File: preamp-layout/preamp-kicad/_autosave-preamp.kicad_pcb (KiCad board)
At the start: 2 copper layers, 431 parts, among them J1 Screw_Terminal_01x03, J10 Conn_01x03_Male, J11 Conn_01x02_Male, J12 Conn_01x02_Male, J13 Conn_01x02_Male, J14 Screw_Terminal_01x03, J15 Conn_01x02_Male, J16 Conn_01x02_Male, J17 Conn_01x02_Female, J18 Conn_01x02_Female, J19 Conn_01x05_Female, J2 Conn_01x02_Female, J20 Conn_01x03_Male, J26 Conn_01x03_Female, J27 Conn_01x03_Female, J28 Conn_01x03_Female, J29 Conn_01x03_Female, J3 Conn_01x02_Female, J30 Conn_01x03_Female, J31 Conn_01x03_Male, J32 Conn_01x03_Male, J35 Conn_01x03_Male, J36 Conn_01x03_Male, J37 Conn_01x03_Male, J38 Conn_01x03_Male, J39 Conn_01x03_Male, J4 Conn_01x02_Male, J40 Conn_01x03_Male, J41 Conn_01x03_Male, J42 Conn_01x03_Female, J43 Conn_01x03_Female, J44 Conn_01x02_Female, J45 Conn_01x07_Female, J46 Conn_01x07_Female, J47 Conn_01x02_Male, J48 Conn_01x02_Male, J49 Conn_01x03_Female, J5 Screw_Terminal_01x03, J50 Conn_01x03_Male, J51 Conn_01x02_Male, J52 Conn_01x03_Female, J53 Conn_01x03_Female, J54 Conn_01x03_Male, J55 Conn_01x02_Male, J56 Conn_01x03_Male, J57 Conn_01x02_Male, J58 Conn_01x03_Male, J59 Conn_01x04_Male, J6 Screw_Terminal_01x03, J60 Conn_01x04_Female, J61 Conn_01x03_Male, J62 Conn_01x03_Male, J64 Conn_01x04_Female, J65 Conn_01x04_Male, J66 Conn_01x03_Male, J67 Conn_01x03_Male, J68 Conn_01x03_Female, J69 Conn_01x03_Male, J7 Screw_Terminal_01x03, J70 XLR3, J71 XLR3, J72 XLR3, J73 XLR3, J74 Conn_01x03_Female, J75 Conn_01x03_Female, J76 Conn_01x03_Female, J77 Conn_01x03_Female, J78 Conn_01x03_Female, J79 Conn_01x03_Female, J8 Conn_01x03_Male, J80 Conn_01x03_Female, J81 Conn_01x03_Female, J82 Conn_01x02_Male, J83 Conn_01x02_Male, J84 Conn_01x05_Female, J9 Conn_01x03_Male, K2 G6JU, K3 G6JU, K4 G6JU, K5 G6JU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

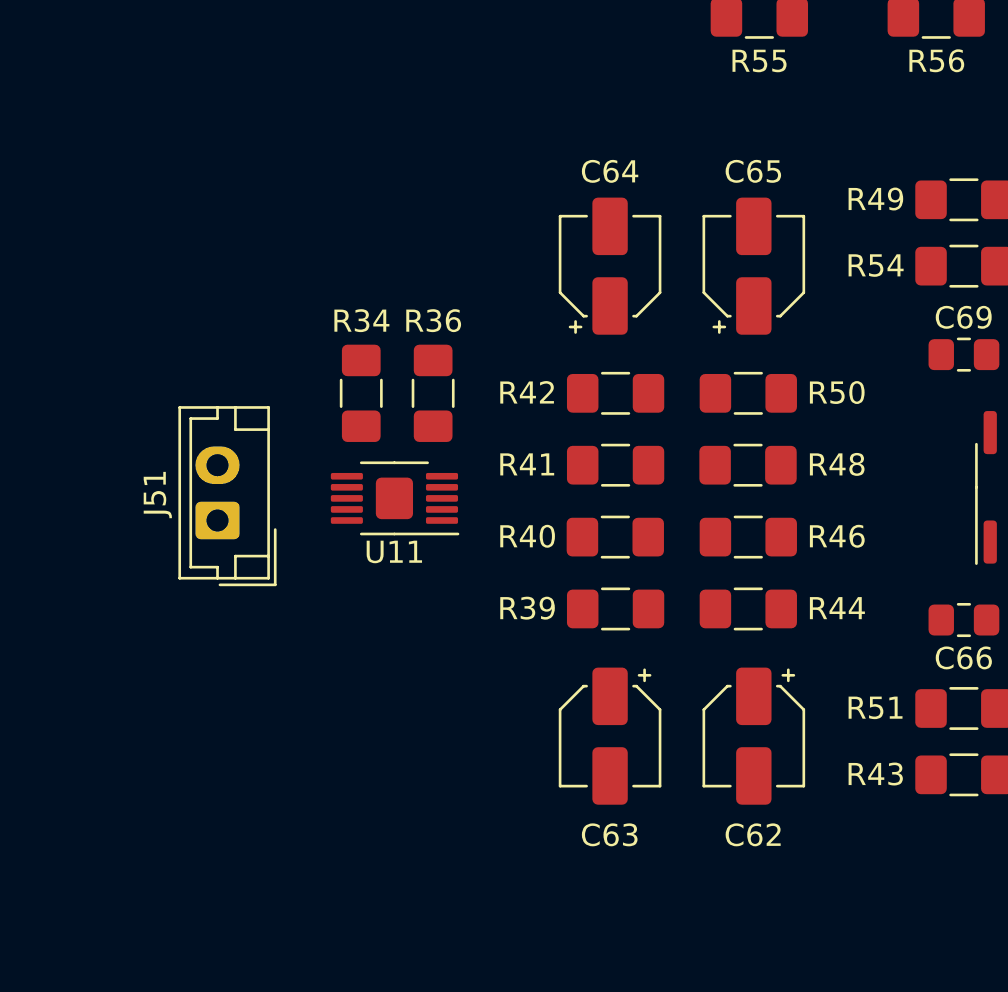
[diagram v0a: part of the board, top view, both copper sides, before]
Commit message: Prelim PCB layout
Work done to lay out PCBs. Saving in anticipation of creating branch with a different input switching topology.
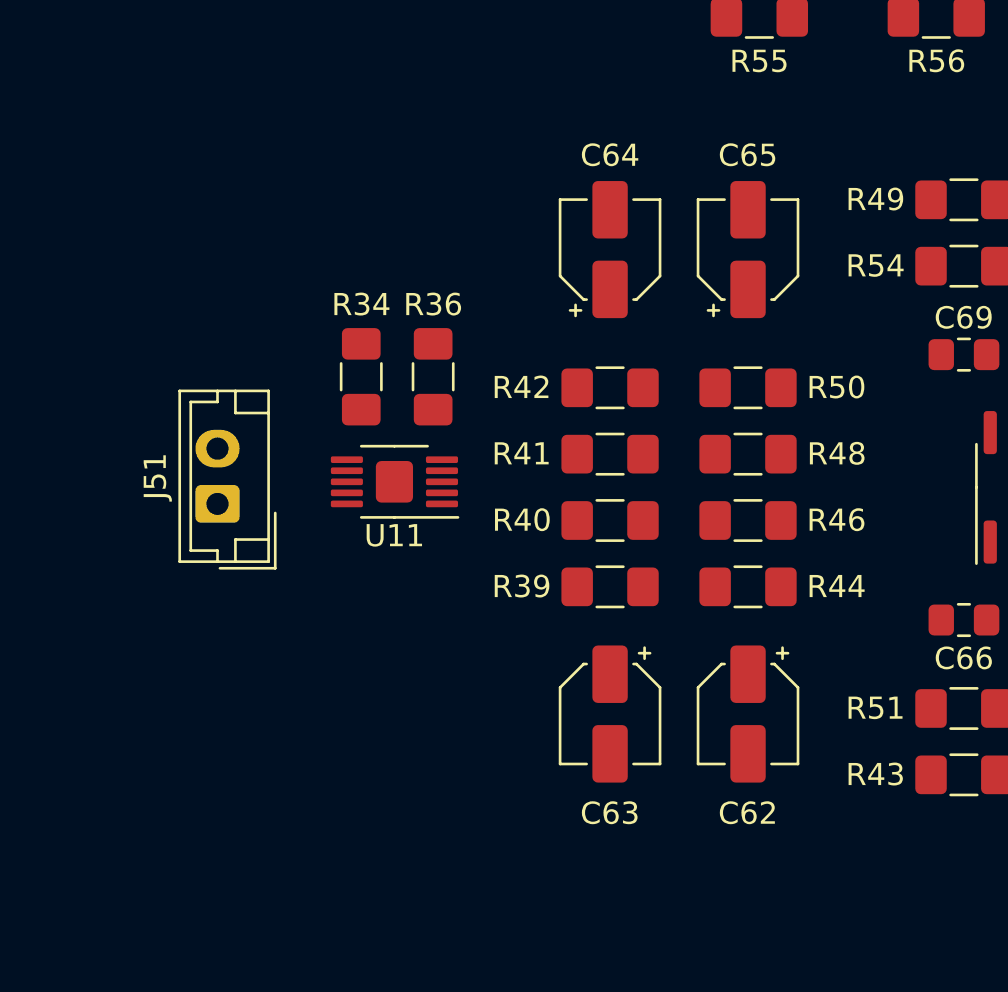
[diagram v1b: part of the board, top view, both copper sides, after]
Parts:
- moved C62 1.03 mm to (302.2, 383.2)
- moved R39 1.03 mm to (296.0, 377.5)
- moved R44 1.00 mm to (302.2, 377.5)
- moved C63 1.00 mm to (296.0, 383.2)
- moved C65 0.79 mm to (302.2, 362.2)
- moved R40 0.79 mm to (296.0, 374.5)
- moved R46 0.75 mm to (302.2, 374.5)
- moved C64 0.75 mm to (296.0, 362.2)
- moved J51 0.75 mm to (278.2, 373.8)
- moved R34 0.75 mm to (284.8, 368.0)
- moved R36 0.75 mm to (288.0, 368.0)
- moved U11 0.75 mm to (286.2, 372.8)
- moved R41 0.56 mm to (296.0, 371.5)
- moved R48 0.50 mm to (302.2, 371.5)
- moved R42 0.35 mm to (296.0, 368.5)
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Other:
- net class 15v_pwr added: clearance 0.5, trace_width 1, via_dia 0.8, via_drill 0.4
- net class 3.3v_pwr added: clearance 0.5, trace_width 1, via_dia 0.8, via_drill 0.4
- net class 5v_pwr added: clearance 0.5, trace_width 1, via_dia 0.8, via_drill 0.4
- net class ac_pwr added: clearance 2, trace_width 4, via_dia 0.8, via_drill 0.4
- net class analog_signal added: clearance 0.5, trace_width 1, via_dia 0.8, via_drill 0.4
- net class digital_signal added: clearance 0.2, trace_width 0.25, via_dia 0.8, via_drill 0.4
